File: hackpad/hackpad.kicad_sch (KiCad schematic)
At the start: 15 parts, among them SW1 SW_Push, SW10 SW_Push, SW2 SW_Push, SW3 SW_Push, SW4 SW_Push, SW5 SW_Push, SW6 SW_Push, SW7 SW_Push, SW9 SW_Push, U1 MOUDLE-SEEEDUINO-XIAO

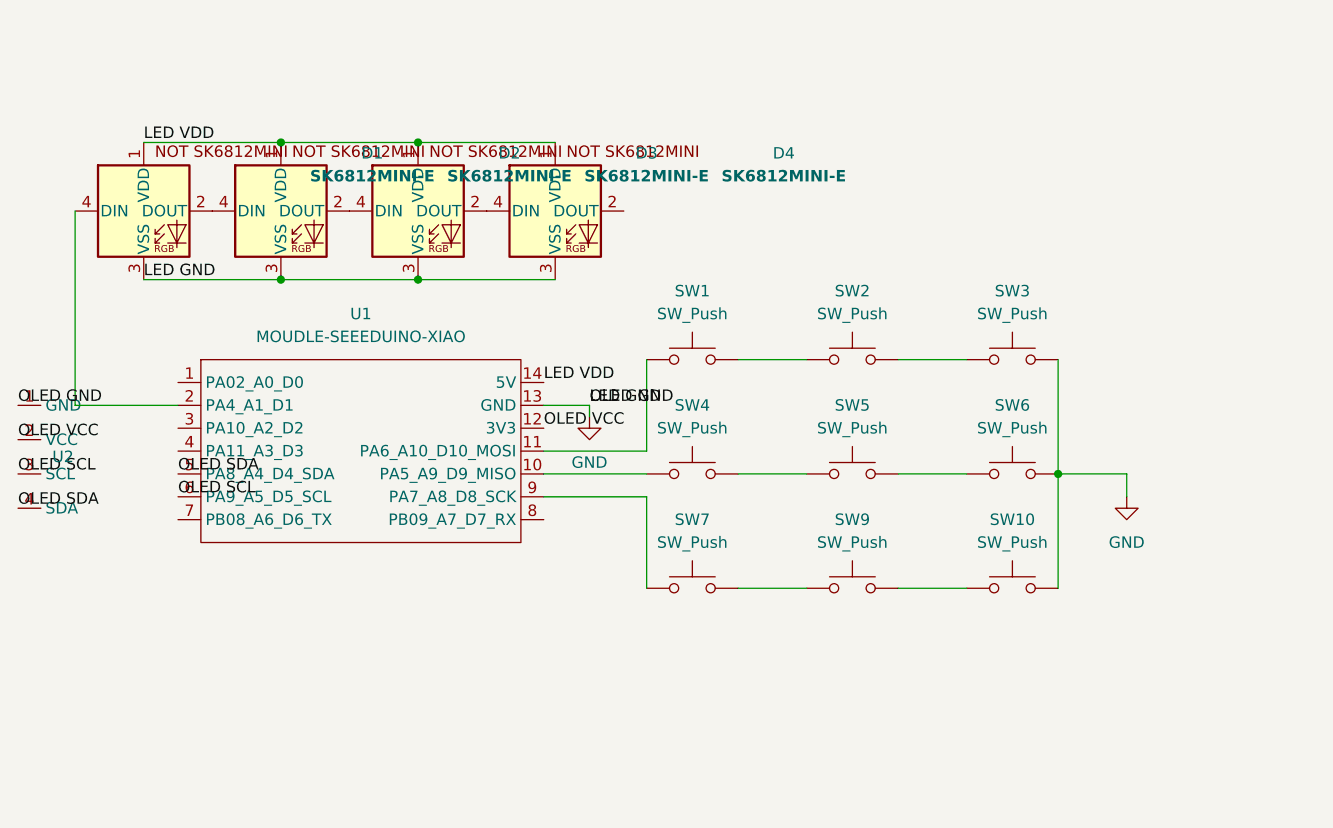
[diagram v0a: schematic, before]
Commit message: Adjusted Firmware for diodes.
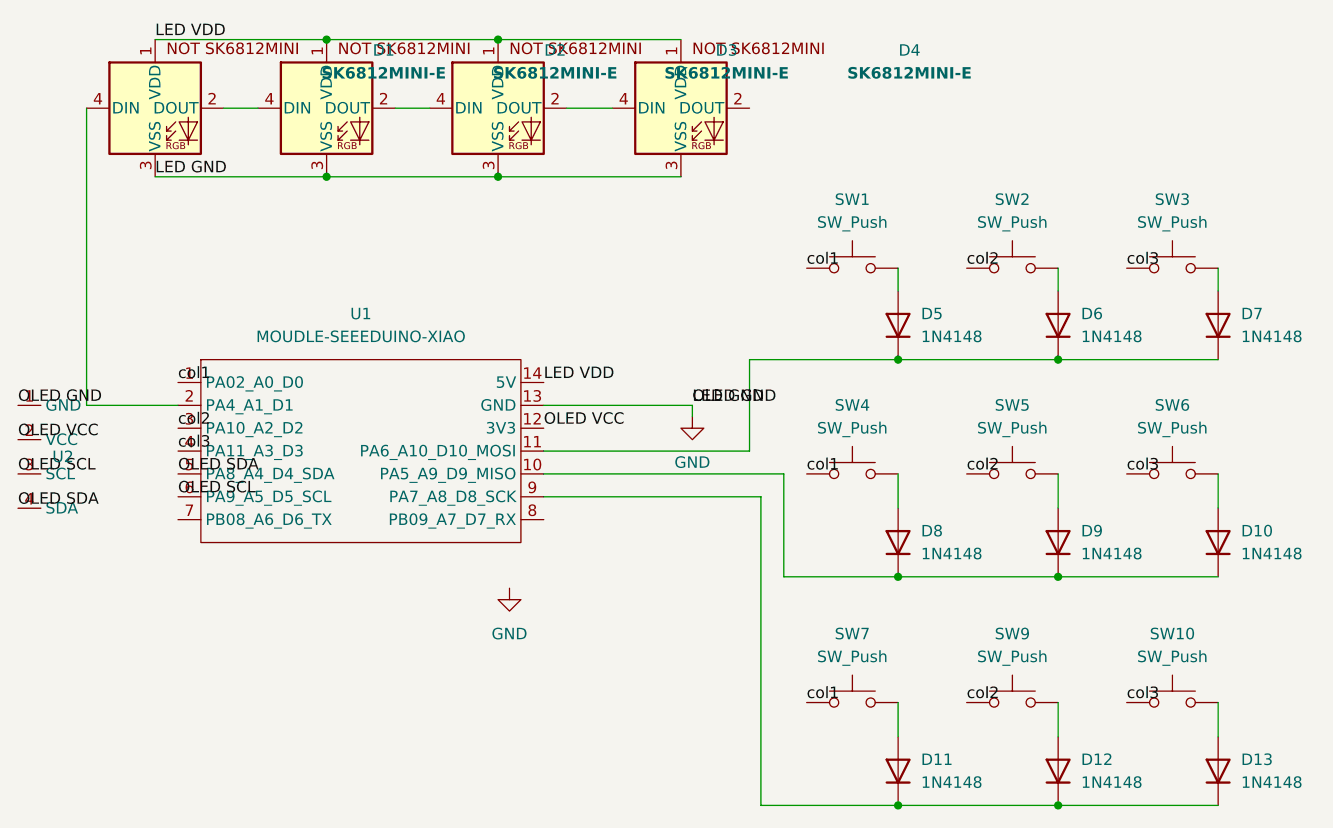
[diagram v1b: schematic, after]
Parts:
- added D10, D11, D12, D13, D5, D6, D7, D8, D9: 1N4148, Diode_THT:D_DO-35_SOD27_P7.62mm_Horizontal, symbol Diode:1N4148
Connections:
- net GND: no longer SW10.2, SW3.2, SW6.2
- net at U1.10 (PA5_A9_D9_MISO): now also D10.1 (K), D8.1 (K), D9.1 (K); no longer SW4.1
- net at SW4.2: now also D8.2 (A); no longer SW5.1
- net at SW1.2: now also D5.2 (A); no longer SW2.1
- net at SW2.2: now also D6.2 (A); no longer SW3.1
- net col1: now reaches U1.1 (PA02_A0_D0)
- net col1: now also SW1.1, SW4.1, SW7.1
- net at U1.11 (PA6_A10_D10_MOSI): now also D5.1 (K), D6.1 (K), D7.1 (K); no longer SW1.1
- net col2: now reaches U1.3 (PA10_A2_D2)
- net col2: now also SW2.1, SW5.1, SW9.1
- net col3: now reaches U1.4 (PA11_A3_D3)
- net col3: now also SW10.1, SW3.1, SW6.1
- net at U1.9 (PA7_A8_D8_SCK): now also D11.1 (K), D12.1 (K), D13.1 (K); no longer SW7.1
- net at SW9.2: now also D12.2 (A); no longer SW10.1
- net at SW7.2: now also D11.2 (A); no longer SW9.1
- net at SW5.2: now also D9.2 (A); no longer SW6.1
- new net: D13.2 (A), SW10.2
- new net: D7.2 (A), SW3.2
- new net: D10.2 (A), SW6.2
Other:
- moved on the sheet: D1, D2, D3, D4, SW1, SW10, SW2, SW3, SW4, SW5, SW6, SW7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
